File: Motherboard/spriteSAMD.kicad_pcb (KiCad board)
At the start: 4 copper layers, 35 x 35 mm, 34 parts, among them IC1 BMX160, J1 Conn_01x01, J2 10118194-0001LF, J28 Conn_01x01, J29 Conn_01x01, J3 Micro_SD_Card, J30 Conn_01x01, J4 xf2m-2415-1a, J5 XF2M-1015-1A, SW1 KMR231NG LFS, U1 RFM95W-915S2, U2 ATSAMD51G_TQFN48, U3 DRV8833PWP, U4 TPS82740BSIPR, U5 DRV8833PWP, U8 RFM95W-915S2, X1 ANTENNA_U.FL, X2 ANTENNA_U.FL

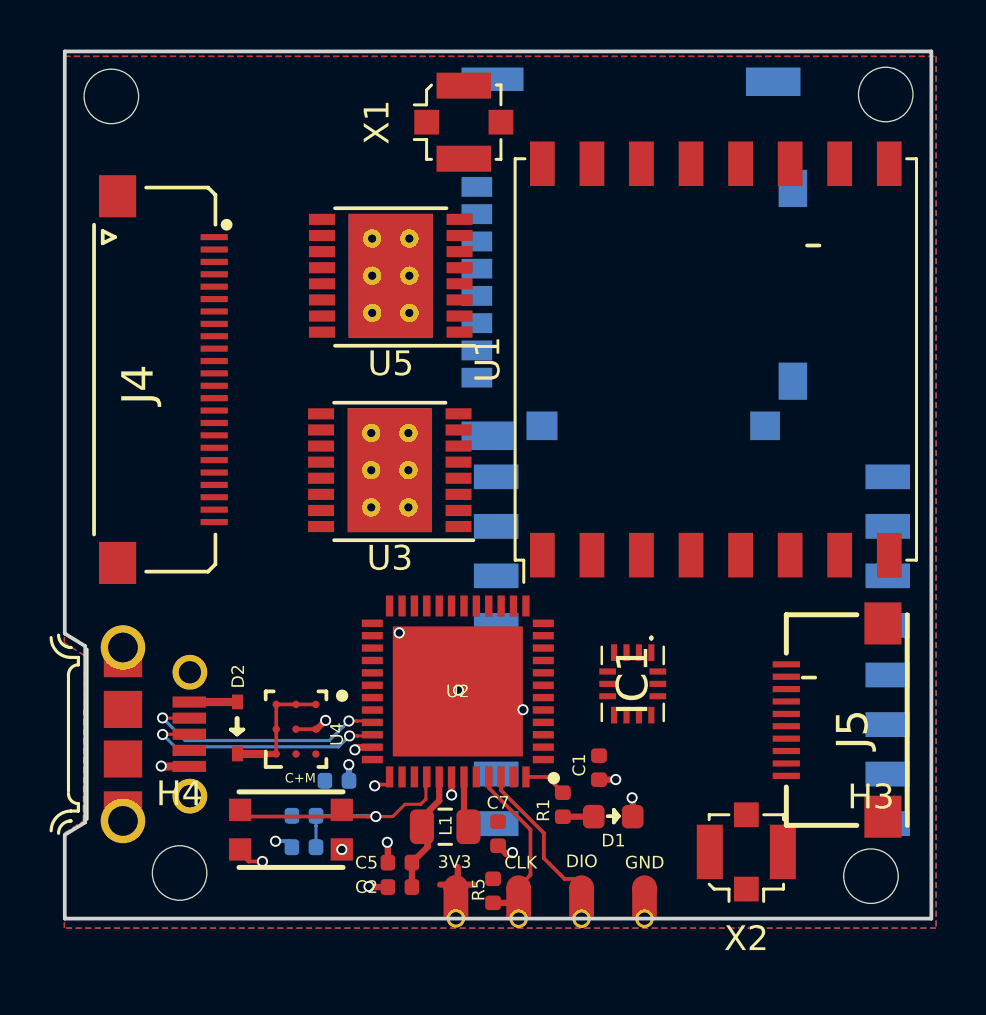
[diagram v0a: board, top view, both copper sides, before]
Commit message: added WDT and took closer-look at fit
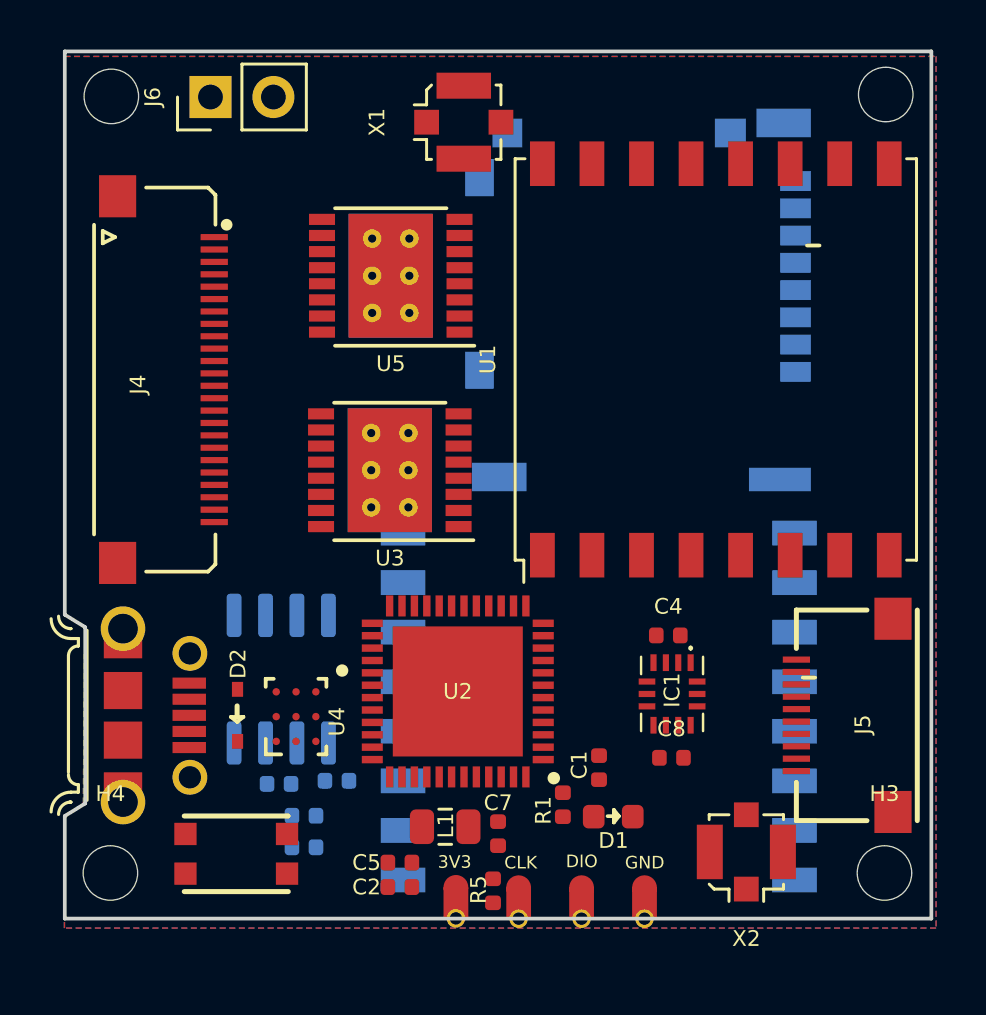
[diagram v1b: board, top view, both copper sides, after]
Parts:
- added C4: 0.1uF, Capacitor_SMD:C_0402_1005Metric, F.Cu at (106.1, 97.6)
- added C8: 0.1uF, Capacitor_SMD:C_0402_1005Metric, F.Cu at (106.2, 102.6)
- added J6: Conn_01x02, Connector_PinHeader_2.54mm:PinHeader_1x02_P2.54mm_Vertical, F.Cu at (87.6, 75.9)
- added R3: 10K, Resistor_SMD:R_0402_1005Metric, B.Cu at (90.4, 103.6)
- added U6: MAX708RESA-T, Package_SO:SO-8_3.9x4.9mm_P1.27mm, B.Cu at (90.5, 99.4)
- moved U8 4.39 mm to (103.3, 100.5)
- moved H4 2.79 mm to (83.6, 107.2)
- moved SW1 2.42 mm to (88.6, 106.4)
- moved J3 2.34 mm to (105.6, 84.1), turned to 90 degrees
- moved IC1 1.64 mm to (106.2, 100.0)
- moved J2 0.76 mm to (84.1, 100.8)
- moved H3 0.56 mm to (114.8, 107.2)
- moved D2 0.51 mm to (88.7, 100.8)
- moved U4 0.51 mm to (91.1, 100.9)
- moved J5 0.45 mm to (111.3, 100.8)
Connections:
- net Net-(C6-Pad2) renamed ~RESET
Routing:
- net ~RESET: track 12.8 -> 0.00 mm, vias 1 -> 0
- net /USB-: track 10.2 -> 0.00 mm, vias 2 -> 0
- net /USB+: track 9.92 -> 0.00 mm, vias 2 -> 0
- net GND: track 8.94 -> 0.00 mm, vias 14 -> 0
- net /SWCLK: track 6.29 -> 0.00 mm
- net /SWDIO: track 6.02 -> 0.00 mm
- net Net-(D2-Pad1): track 5.16 -> 0.00 mm
- net Net-(C2-Pad1): track 4.97 -> 0.00 mm
- net +3V3: track 3.60 -> 0.00 mm, vias 2 -> 0
- net Net-(L1-Pad1): track 2.04 -> 0.00 mm
- net VUSB: track 1.95 -> 0.00 mm
- net /LED1: track 1.76 -> 0.00 mm
- net Net-(D1-Pad1): track 1.25 -> 0.00 mm
- net Net-(U2-Pad37): track 0.91 -> 0.00 mm, vias 1 -> 0
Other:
- outline, holes or cut-outs redrawn
- net class Default: trace_width 0.0889 -> 0.127
- net class PCC removed
- net class PWR removed
- rule pad_to_mask_clearance: 0.0254 -> 0.0508
- rule trace_min: 0.0889 -> 0.127
- rule via_min_drill: 0.25 -> 0.3
- board text removed: "C+M"

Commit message: labeled schematic in case anyone ends up seeing this
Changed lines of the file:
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@@
   (general
     (thickness 1.2)
-    (drawings 28)
+    (drawings 27)
     (tracks 0)
     (zones 0)
@@
     (effects (font (size 0.508 0.508) (thickness 0.0889)))
   )
-  (gr_line (start 111.68 81.875) (end 112.188 81.875) (layer F.SilkS) (width 0.15))
   (gr_circle (center 92.91828 99.02952) (end 92.97924 99.03968) (layer F.SilkS) (width 0.15))
   (gr_circle (center 92.91828 99.02952) (end 93.06814 99.11842) (layer F.SilkS) (width 0.15))
